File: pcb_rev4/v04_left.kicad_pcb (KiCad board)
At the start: 2 copper layers, 169.1 x 135.1 mm, 74 parts, among them J1 Audio-Jack-4, SW1 SW_Push, U1 ProMicro

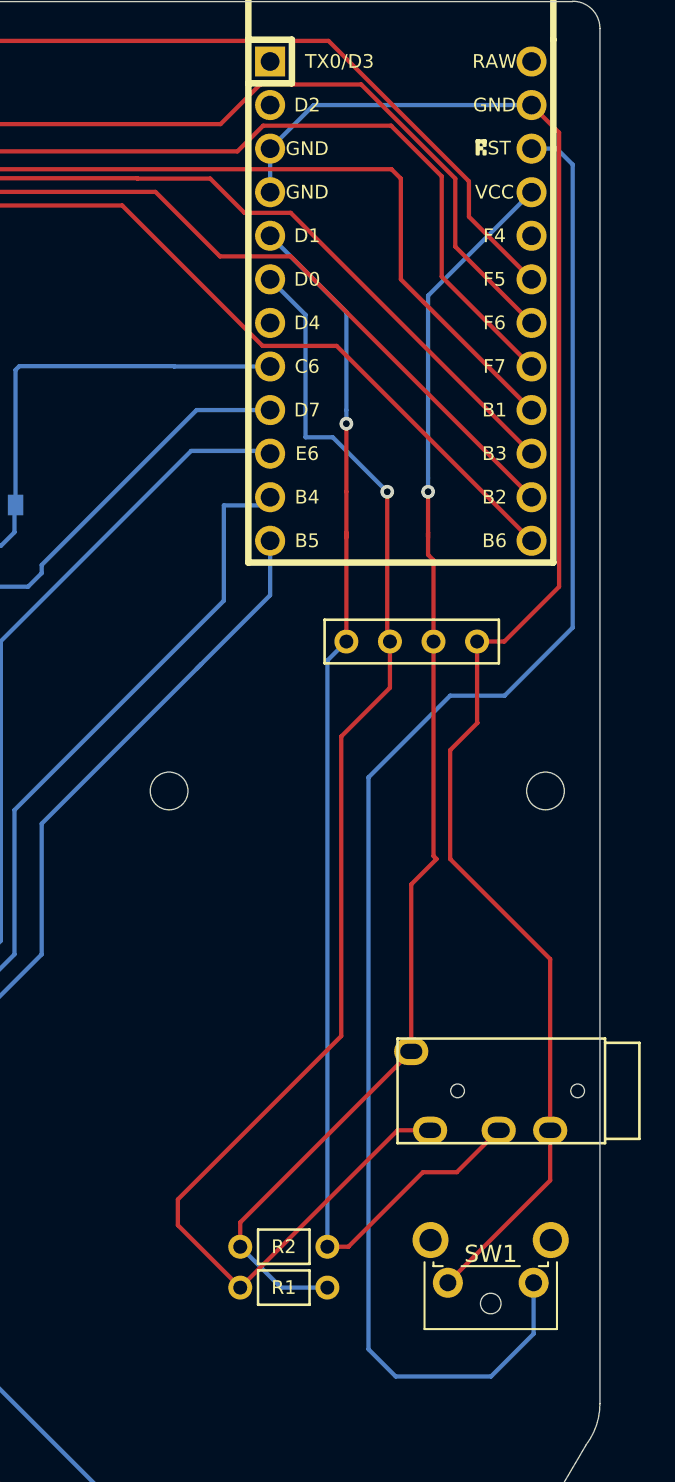
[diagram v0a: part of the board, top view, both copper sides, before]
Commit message: Fixed footprint for TRRS jack in left side and rerouted.
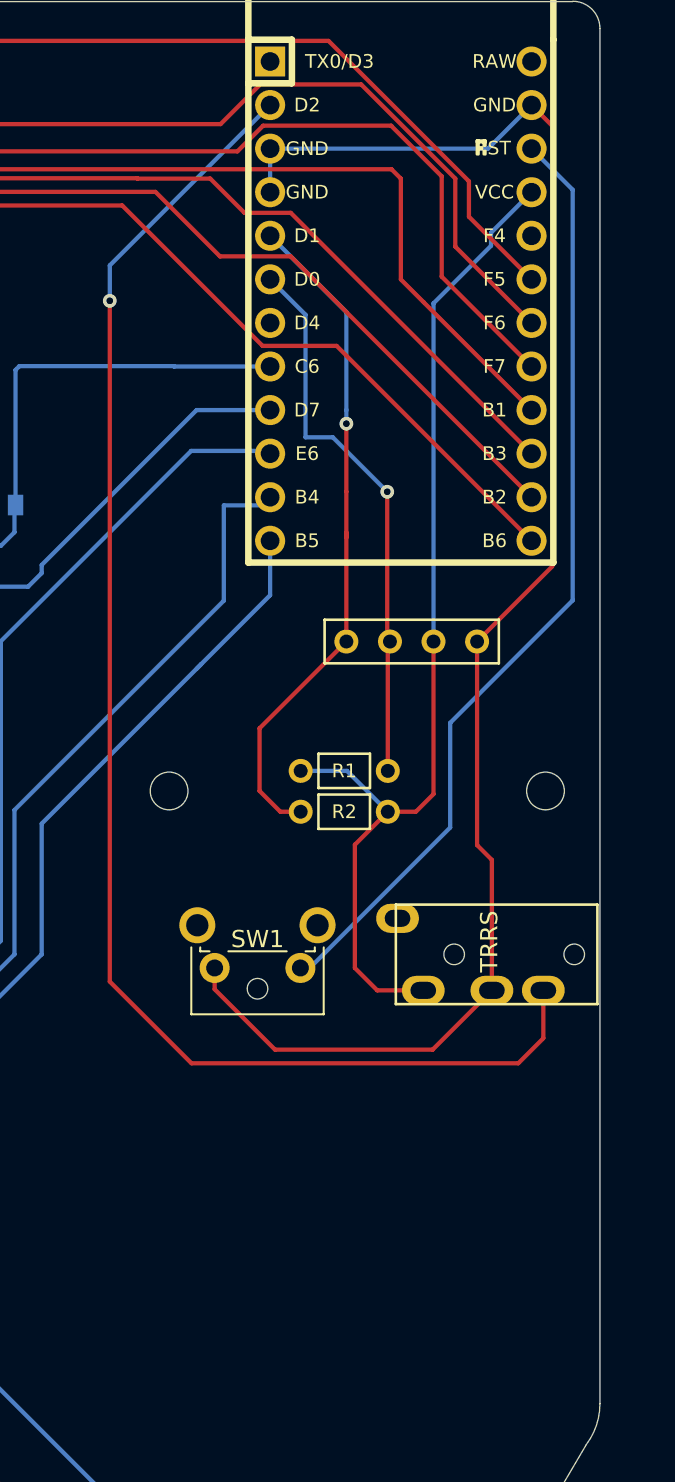
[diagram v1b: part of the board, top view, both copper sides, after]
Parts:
- removed J1: Audio-Jack-4, Keebio-Parts:TRRS-PJ-320A
- added TRRS1: MJ-4PP-9, kbd:MJ-4PP-9_1side, F.Cu at (5.56, 60.3)
- moved R1 30.3 mm to (-9.35, 49.6), turned to 180 degrees
- moved R2 25.6 mm to (-9.35, 52.0), turned to 0 degrees
- moved SW1 22.8 mm to (-11.9, 61.1)
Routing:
- net DATA: track 0.00 -> 85.6 mm, vias 0 -> 1
- net SCL: track 84.1 -> 32.5 mm
- net RESET: track 92.9 -> 55.7 mm
- net SDA: track 74.3 -> 39.5 mm
- net VCC: track 75.3 -> 61.0 mm, vias 1 -> 0
- net GND: track 96.6 -> 93.4 mm

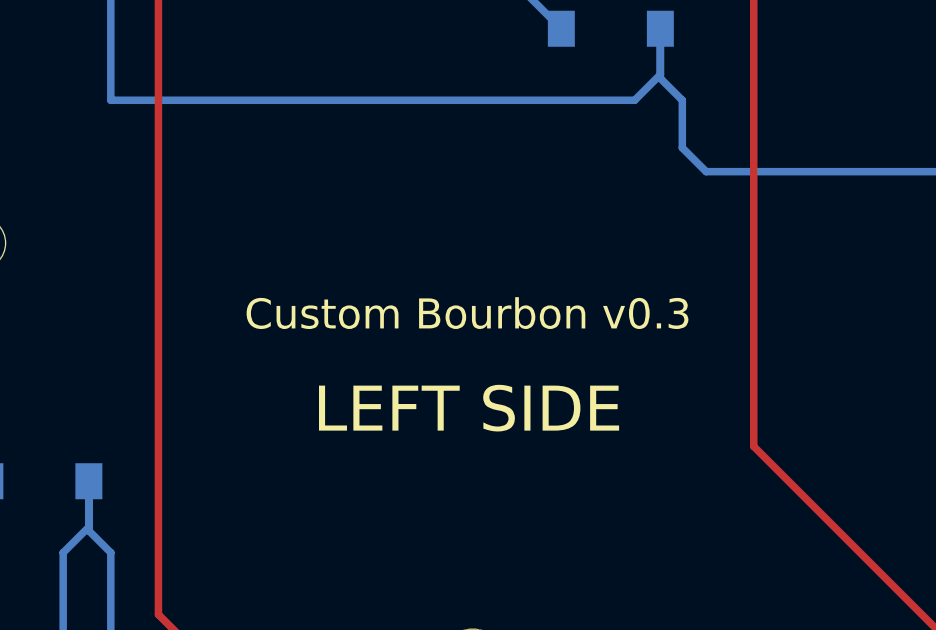
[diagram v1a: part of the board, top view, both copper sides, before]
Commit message: Updated silks for v0.4
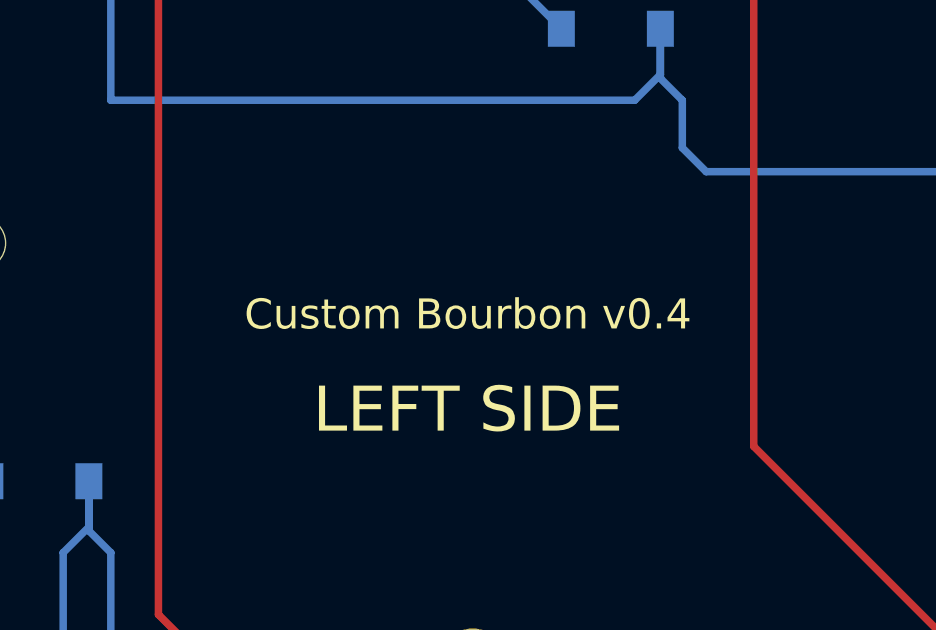
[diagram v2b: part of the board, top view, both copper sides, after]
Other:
- board text added: "Custom Bourbon v0.4"
- board text removed: "Custom Bourbon v0.3"

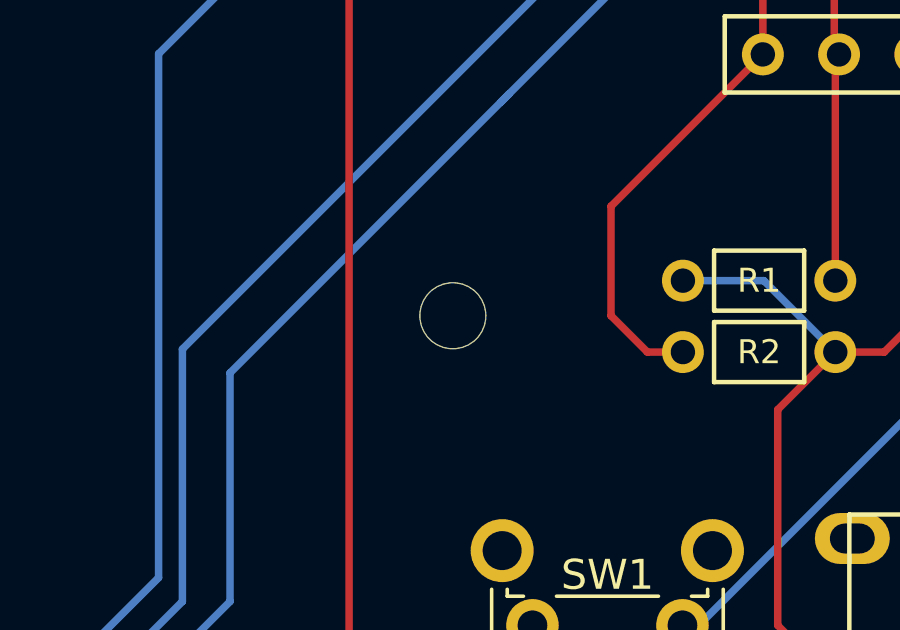
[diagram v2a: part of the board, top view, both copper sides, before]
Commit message: Moved the OLED cover holes slightly for better fit
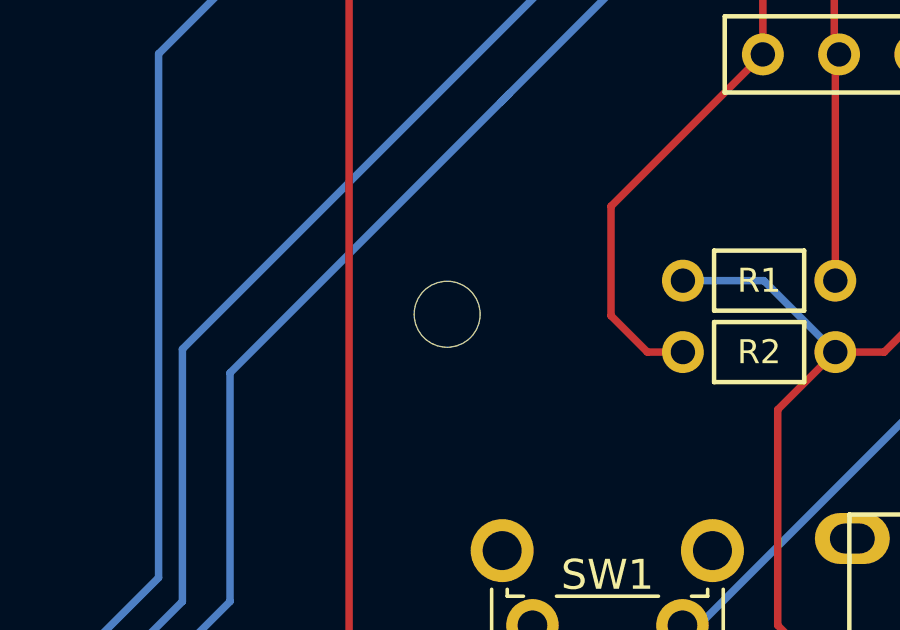
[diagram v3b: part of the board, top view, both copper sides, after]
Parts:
- moved H2 0.20 mm to (-19.8, 50.8)
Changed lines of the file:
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@@
   )
   (module Lily58-footprint:HOLE_M2 (layer F.Cu)
-    (at -19.56 50.8)
+    (at -19.75 50.75)
     (fp_text reference H2 (at 0 -2) (layer Eco2.User) hide
       (effects (font (size 0.29972 0.29972) (thickness 0.07493)))

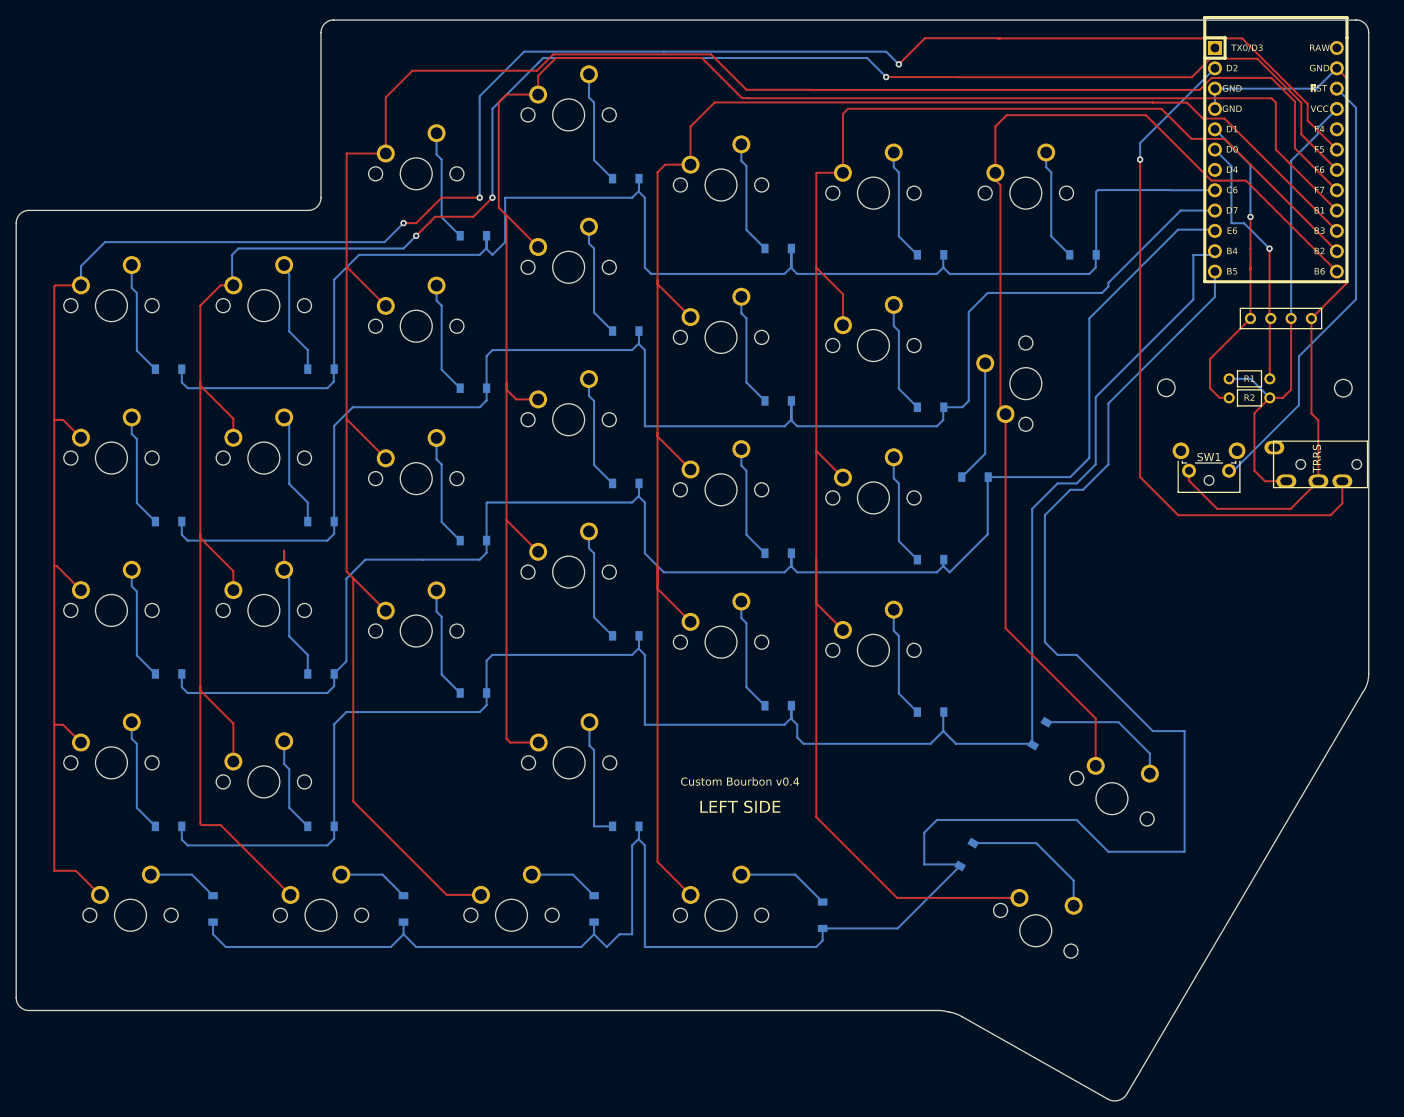
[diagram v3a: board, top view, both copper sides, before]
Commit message: Repositioned both thumb clusters; fixed positioning of z key on left side
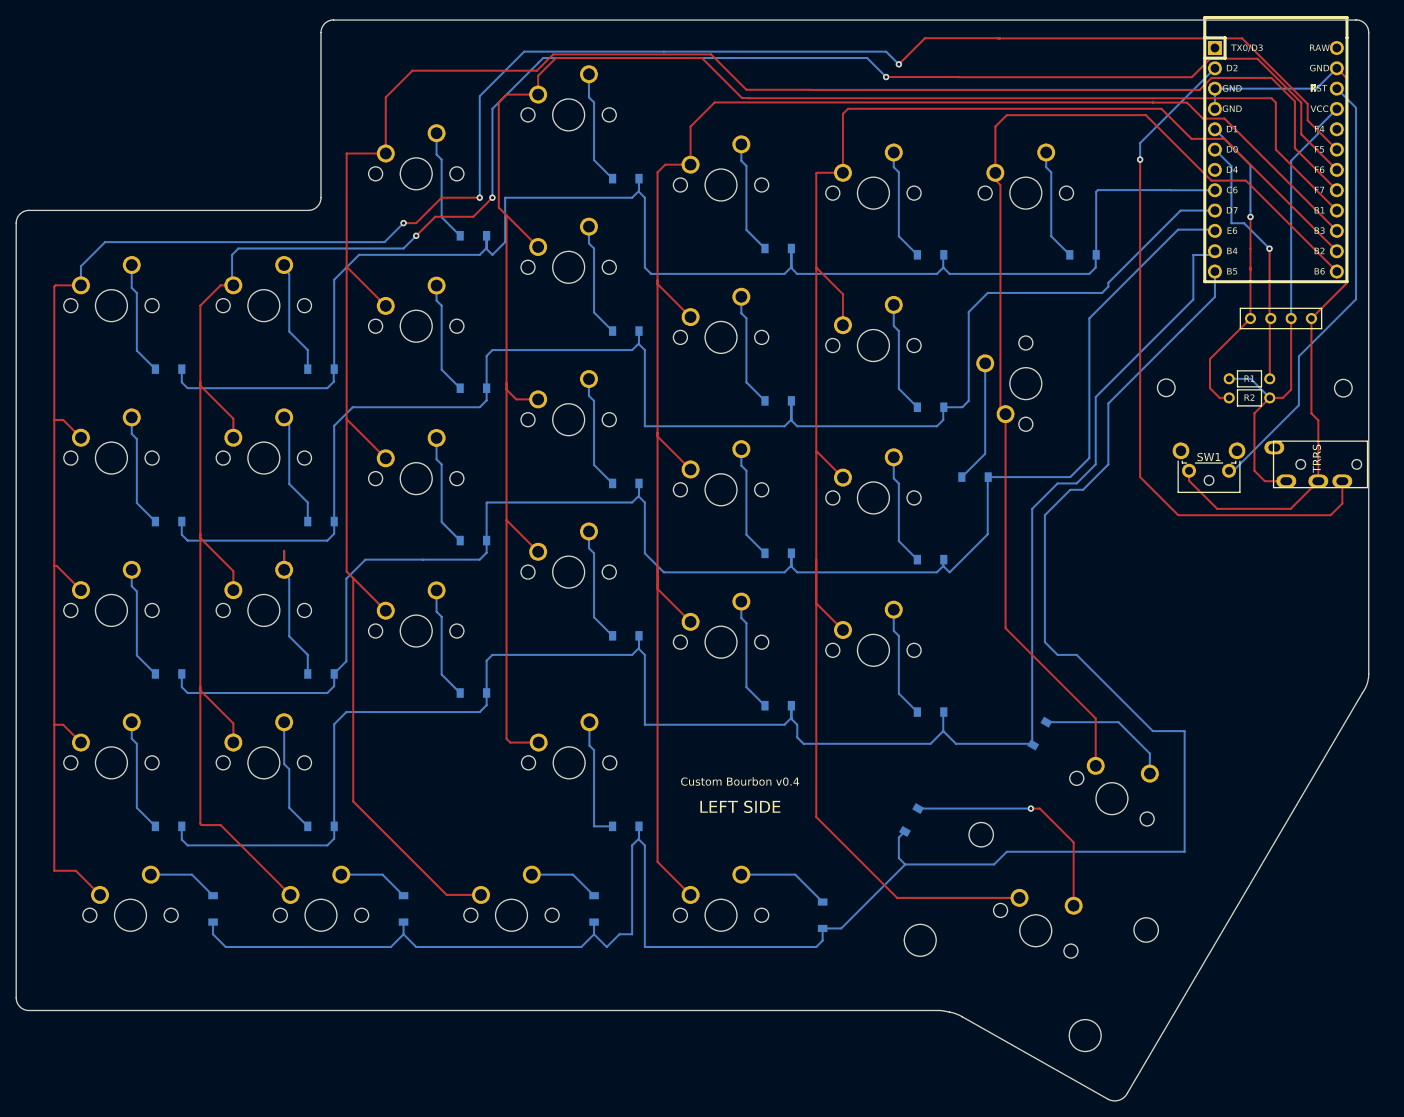
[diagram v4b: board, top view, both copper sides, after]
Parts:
- MX45: footprint MX_Only:MXOnly-1.5U-NoLED -> MX_Only:MXOnly-2U-NoLED
- moved D45 8.13 mm to (-51.6, 104.8)
- moved MX31 2.38 mm to (-132.6, 97.6)
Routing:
- net Net-(D45-Pad2): track 17.6 -> 29.1 mm, vias 0 -> 1
- net row4: track 271.8 -> 261.8 mm
- net Net-(D31-Pad2): track 11.9 -> 14.2 mm
- net col1: track 281.9 -> 279.5 mm
